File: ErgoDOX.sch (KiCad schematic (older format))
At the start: 92 parts, among them J1 USB, J2 3.5mm, J3 JMP, J4 JMP, SW0:10 SW0:3, SW0:11 SW0:2, SW0:12 SW0:1, SW0:7 SW0:6, SW0:8 SW0:5, SW0:9 SW0:4, SW1:10 SW1:3, SW1:11 SW1:2, SW1:12 SW1:1, SW1:13 SW1:0, SW1:9 SW1:4, SW2:10 SW2:3, SW2:11 SW2:2, SW2:12 SW2:1, SW2:13 SW2:0, SW2:7 SW2:6, SW2:8 SW2:5, SW2:9 SW2:4, SW3:10 SW3:3, SW3:11 SW3:2, SW3:12 SW3:1, SW3:13 SW3:0, SW3:8 SW3:5, SW3:9 SW3:4, SW4:10 SW4:3, SW4:11 SW4:2, SW4:12 SW4:1, SW4:13 SW4:0, SW4:7 SW4:6, SW4:8 SW4:5, SW4:9 SW4:4, SW5:10 SW5:3, SW5:11 SW5:2, SW5:12 SW5:1, SW5:13 SW5:0, SW5:7 SW5:6, SW5:8 SW5:5, SW5:9 SW5:4, U1 TEENSY2.0, U2 MCP23018

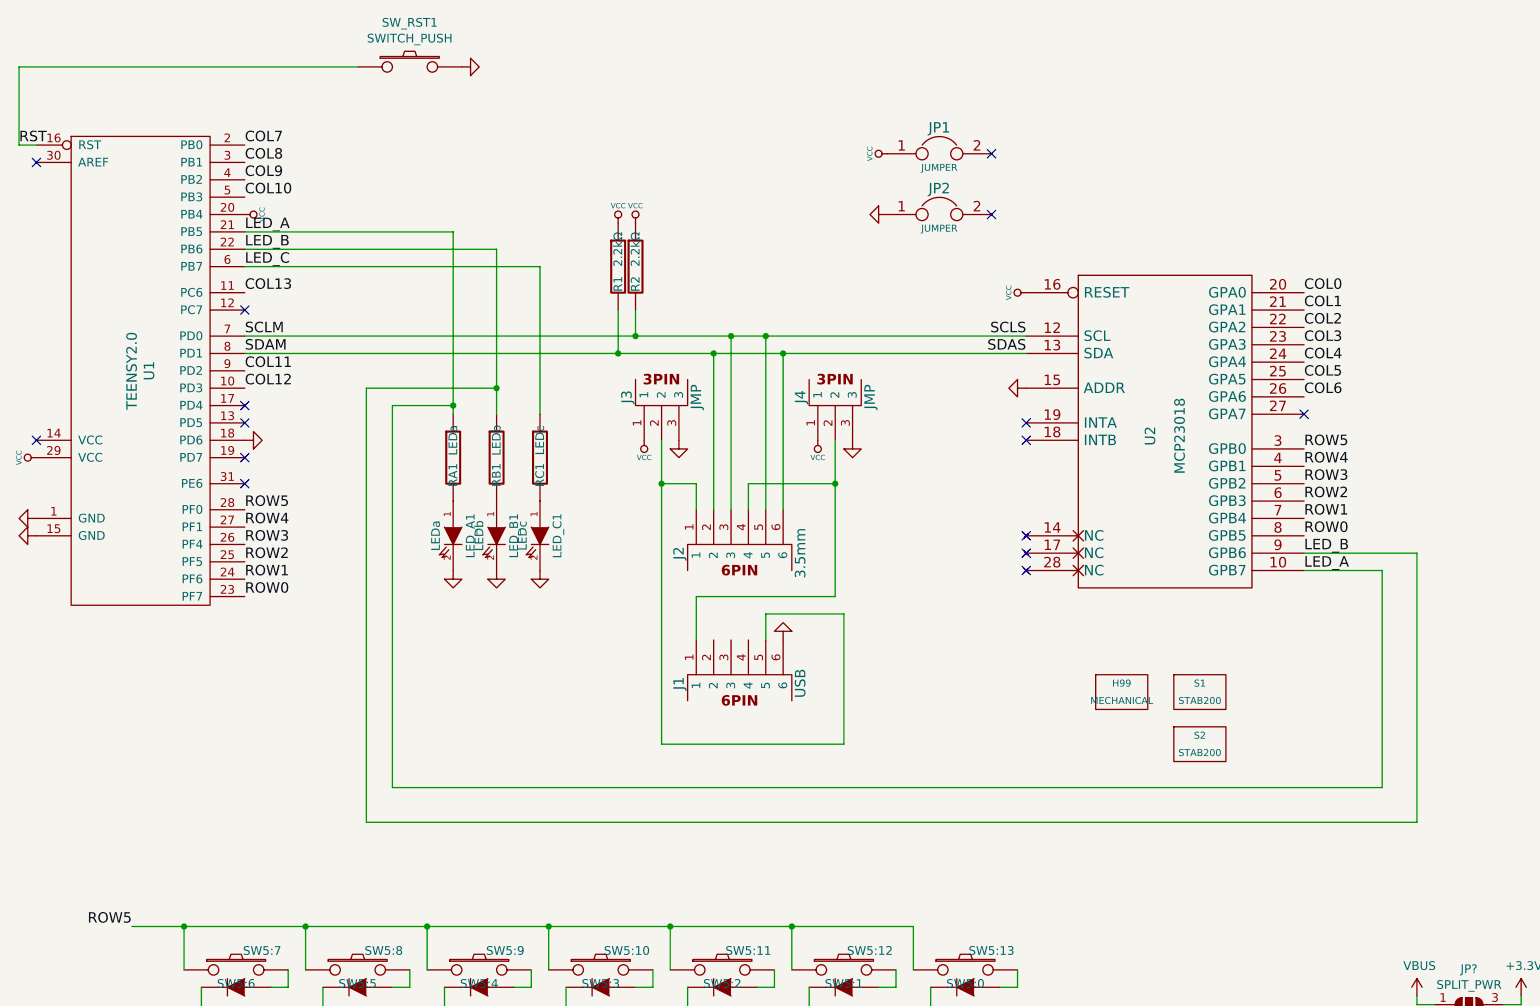
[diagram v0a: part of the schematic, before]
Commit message: Assign footprints to old and new components.
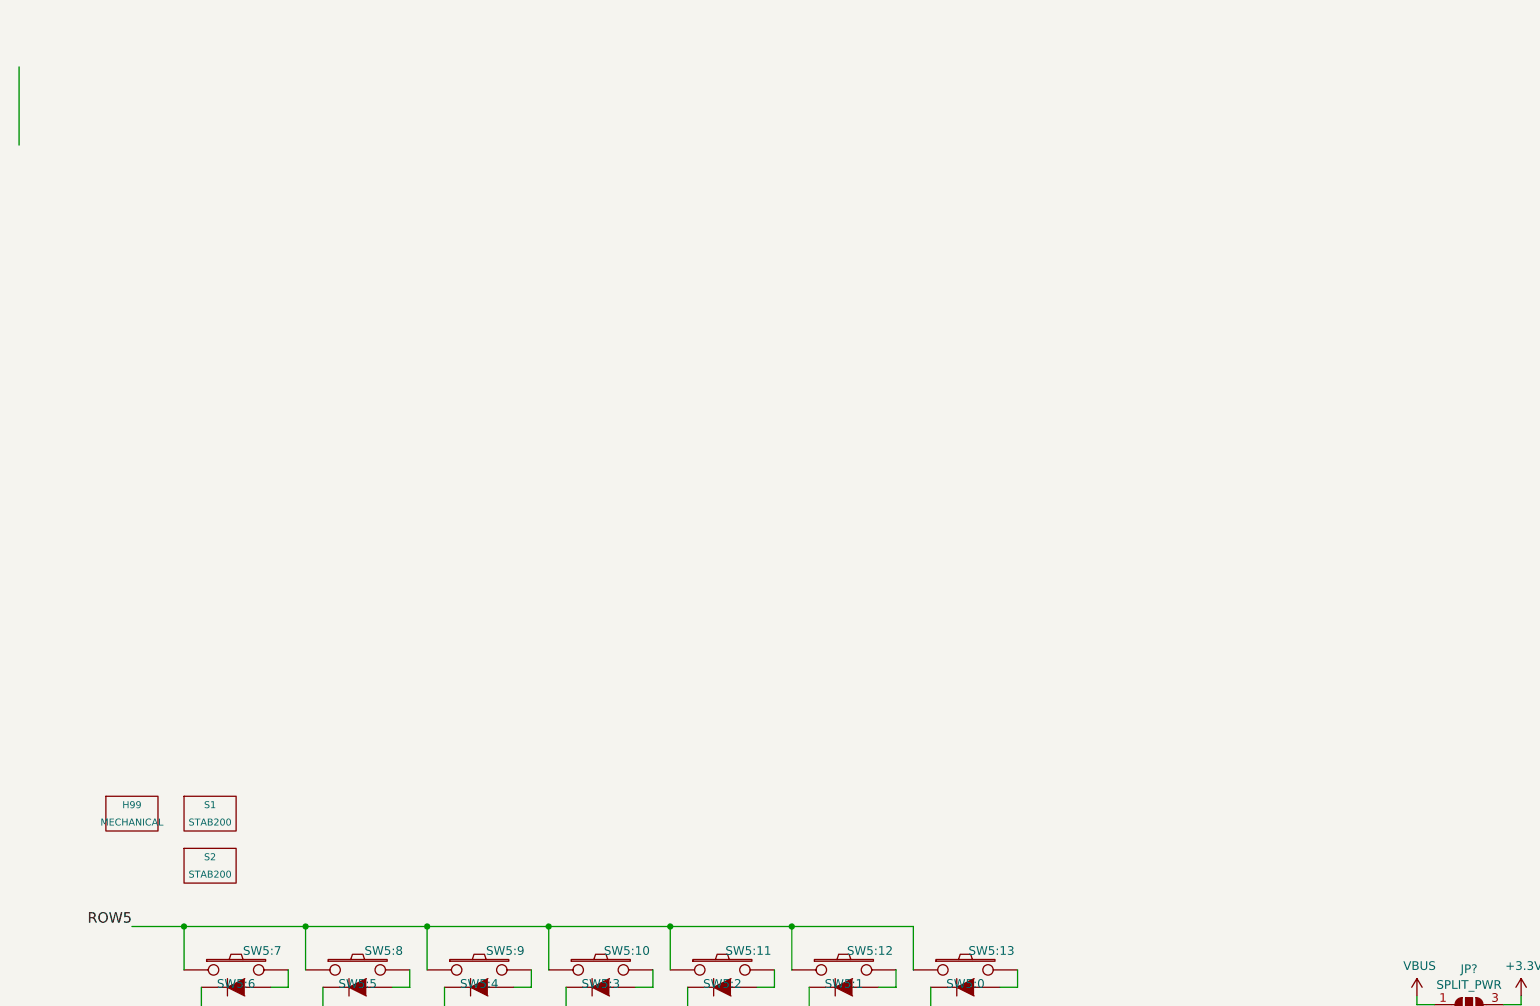
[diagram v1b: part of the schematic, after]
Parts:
- removed J1: USB, symbol component:6PIN
- removed J2: 3.5mm, symbol component:6PIN
- removed J3, J4: JMP, symbol component:3PIN
- removed JP1, JP2: JUMPER, symbol component:JUMPER
- removed LED_A1: LEDa, symbol component:LED
- removed LED_B1: LEDb, symbol component:LED
- removed LED_C1: LEDc, symbol component:LED
- removed R1, R2: 2.2kΩ, symbol component:RESISTOR
- removed RA1: LEDa, symbol component:RESISTOR
- removed RB1: LEDb, symbol component:RESISTOR
- removed RC1: LEDc, symbol component:RESISTOR
- removed SW_RST1: SWITCH_PUSH, Buttons_Switches_SMD:SW_SPST_B3U-1000P, symbol component:SWITCH_PUSH
- removed U1: TEENSY2.0, symbol component:TEENSY2.0
- removed U2: MCP23018, symbol component:MCP23018
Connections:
- no-connect marks 29 -> 14
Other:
- moved on the sheet: H99, S1, S2

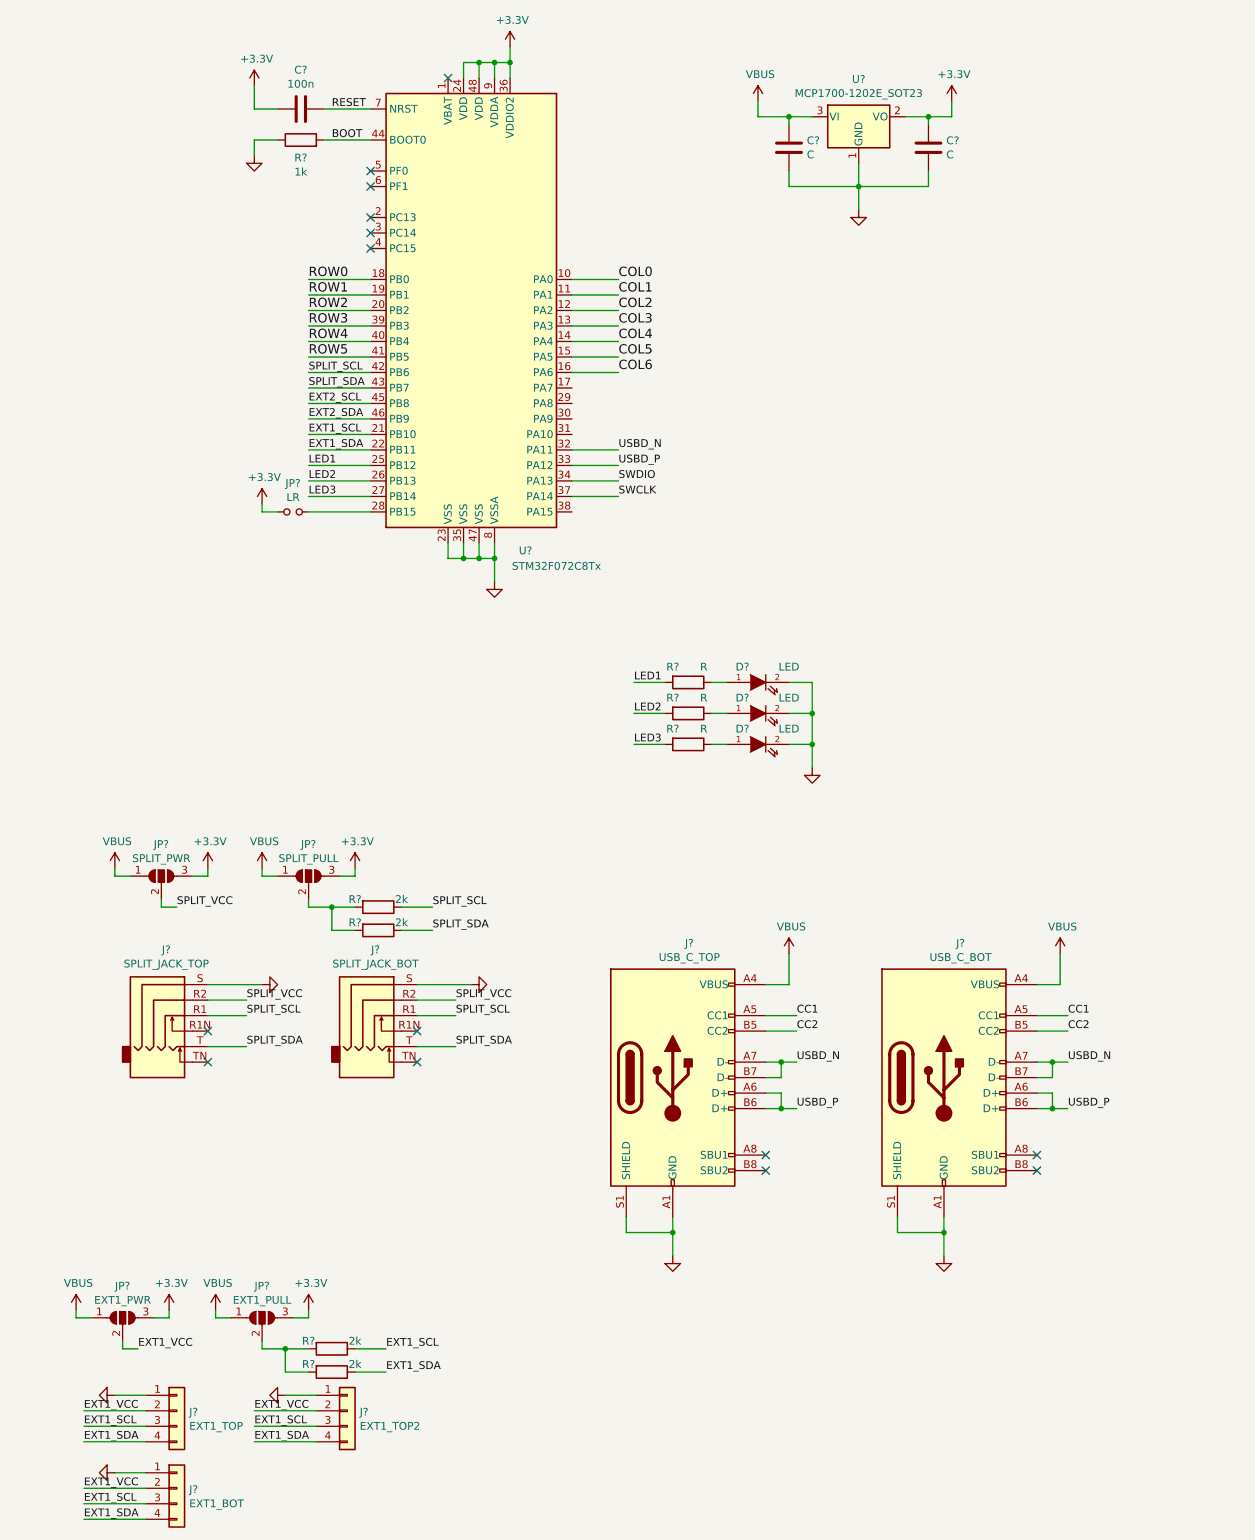
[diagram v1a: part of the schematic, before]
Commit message: Routing done, needs review.
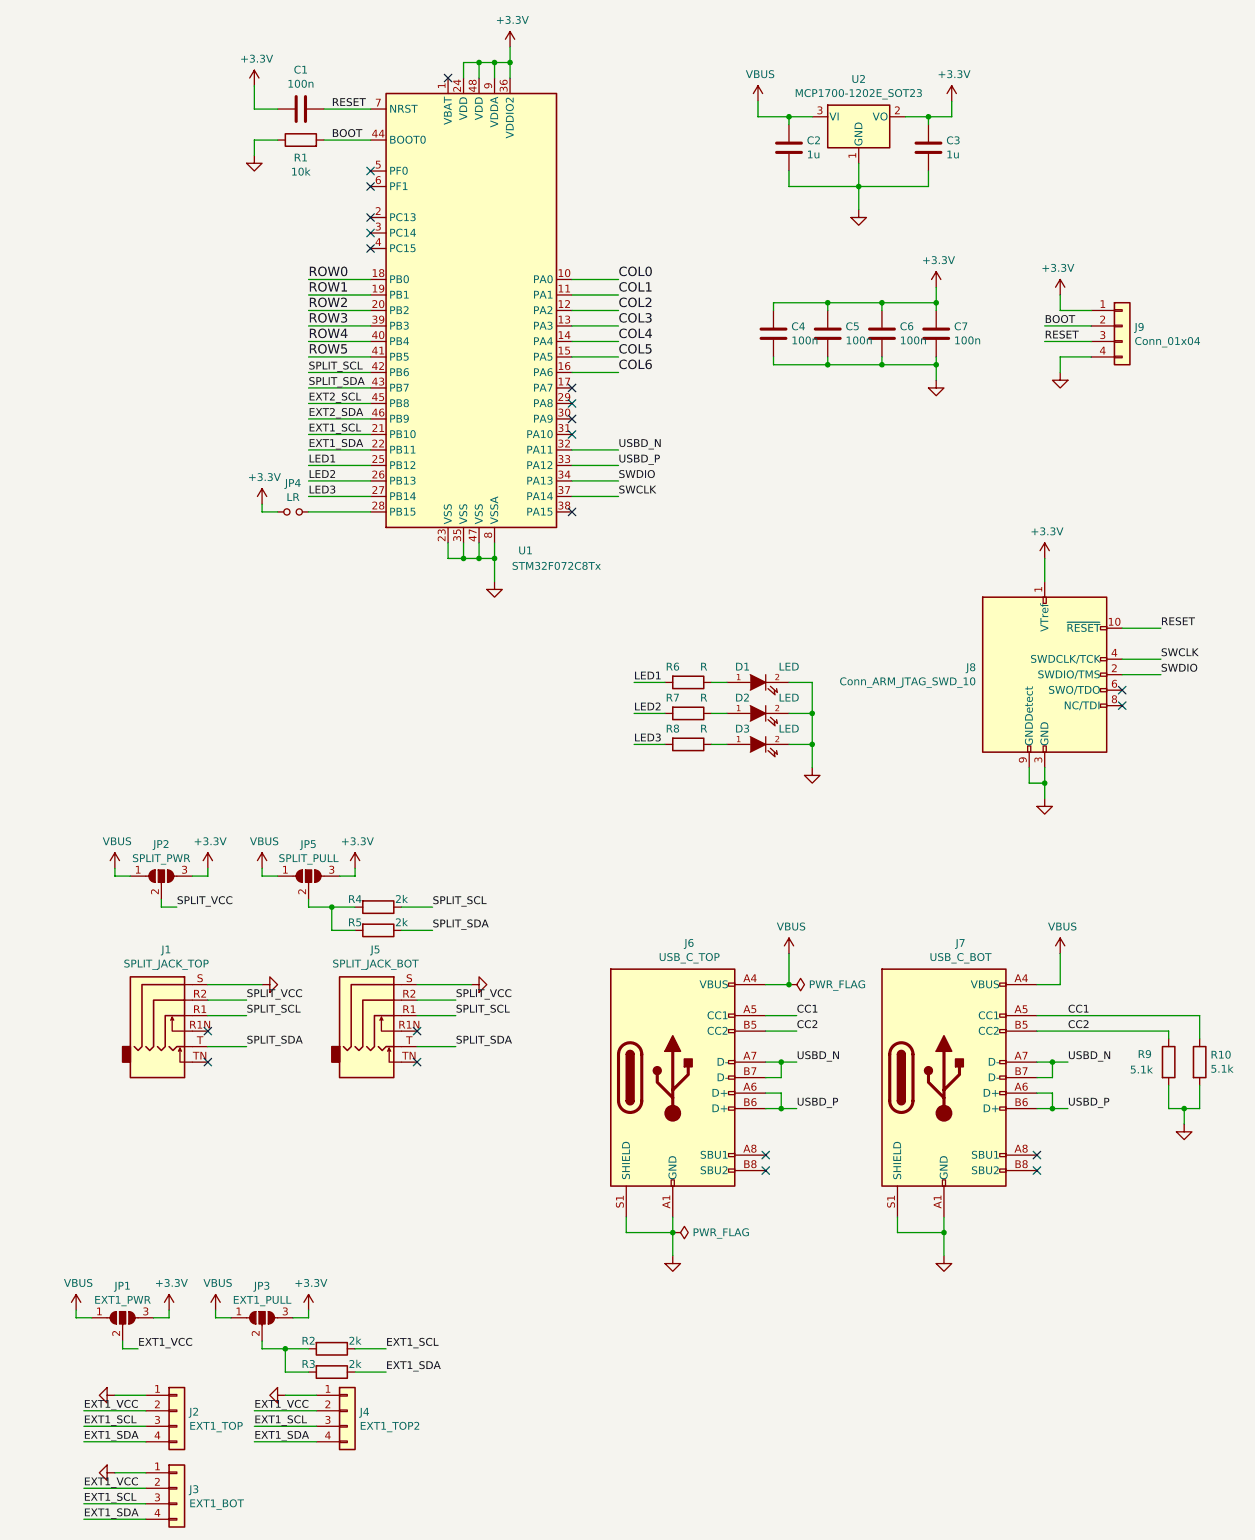
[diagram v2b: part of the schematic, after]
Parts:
- added C4, C5, C6, C7: 100n, Capacitor_SMD:C_0603_1608Metric, symbol Device:C
- added J8: Conn_ARM_JTAG_SWD_10, Connector_PinHeader_1.27mm:PinHeader_2x05_P1.27mm_Vertical_SMD, symbol Connector:Conn_ARM_JTAG_SWD_10
- added J9: Conn_01x04, Connector_PinHeader_2.54mm:PinHeader_1x04_P2.54mm_Horizontal, symbol Connector_Generic:Conn_01x04
- added R10, R9: 5.1k, Resistor_SMD:R_0603_1608Metric, symbol Device:R
- C1: renamed from C?; footprint (none) -> Capacitor_SMD:C_0603_1608Metric
- C2, C3: renamed from C?; value C -> 1u; footprint (none) -> Capacitor_SMD:C_0805_2012Metric
- D1, D2, D3: renamed from D?; footprint (none) -> LED_SMD:LED_0603_1608Metric
- D1:7, D1:8: footprint (none) -> footprint:DIODE
- H99: footprint (none) -> footprint:ErgoDOXmech
- J1, J5: renamed from J?; footprint (none) -> Connector_Audio:Jack_3.5mm_PJ31060-I_Horizontal
- J2, J3: renamed from J?; footprint (none) -> Connector_PinHeader_2.54mm:PinHeader_1x04_P2.54mm_Vertical
- J4: renamed from J?; footprint (none) -> Connector_Molex:Molex_PicoBlade_53047-0410_1x04_P1.25mm_Vertical
- J6, J7: renamed from J?; footprint (none) -> Connector_USB:USB_C_Receptacle_XKB_U262-16XN-4BVC11
- JP1, JP2, JP3, JP5: renamed from JP?; footprint (none) -> Jumper:SolderJumper-3_P2.0mm_Open_TrianglePad1.0x1.5mm
- JP4: renamed from JP?; footprint (none) -> Jumper:SolderJumper-2_P1.3mm_Open_TrianglePad1.0x1.5mm
- R1: renamed from R?; value 1k -> 10k; footprint (none) -> Resistor_SMD:R_0603_1608Metric
- R2, R3, R4, R5, R6, R7, R8: renamed from R?; footprint (none) -> Resistor_SMD:R_0603_1608Metric
- SW0:10, SW0:11, SW0:12, SW0:7, SW0:8, SW0:9, SW1:10, SW1:11, SW1:12, SW1:13, SW1:9, SW2:10, SW2:11, SW2:12, SW2:7, SW2:8, SW2:9, SW3:10, SW3:11, SW3:12, SW3:8, SW3:9, SW4:10, SW4:11, SW4:12, SW4:7, SW4:8, SW4:9, SW5:10, SW5:11, SW5:12, SW5:7, SW5:8, SW5:9: footprint (none) -> ErgoDOX pcb:MX_FLIP_DIODE
- SW2:13, SW3:13, SW4:13, SW5:13: footprint (none) -> ErgoDOX pcb:MX_FLIP_XX
- SX0:10, SX0:11, SX1:7, SX1:8: footprint (none) -> footprint:MX_FLIP
- gave numbers to parts that had none: 2
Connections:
- net +3V3: now also C4.1, C5.1, C6.1, C7.1, J8.1 (VTref), J9.1 (Pin_1)
- net BOOT: now also J9.2 (Pin_2)
- net CC1: now also R10.1
- net CC2: now also R9.1
- net GND: now also C4.2, C5.2, C6.2, C7.2, J8.3 (GND), J8.5 (GND), J8.9 (GNDDetect), J9.4 (Pin_4), R10.2, R9.2
- net RESET: now also J8.10 (~RESET~), J9.3 (Pin_3)
- net SWCLK: now also J8.4 (SWDCLK/TCK)
- net SWDIO: now also J8.2 (SWDIO/TMS)
- no-connect marks 14 -> 21
